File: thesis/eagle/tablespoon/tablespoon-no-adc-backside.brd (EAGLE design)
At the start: 106.3 x 71.1 mm, 35 parts, among them IC1 7805DT, IC2 7805DT, IC3 TL072D, U2 ADCS7477

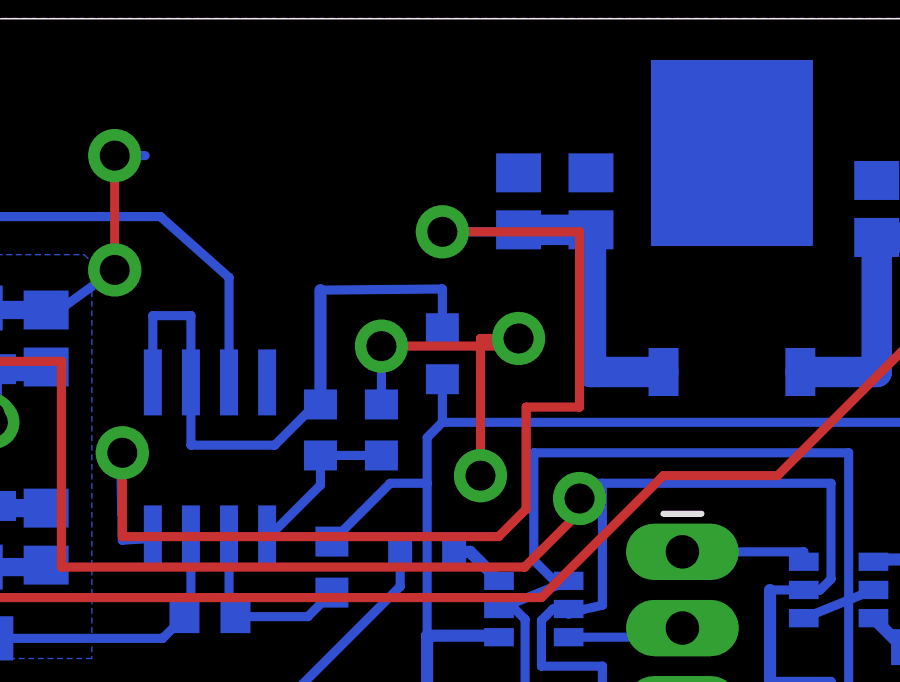
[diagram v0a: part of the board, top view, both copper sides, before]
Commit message: fixed lack of resistor divider on current amp
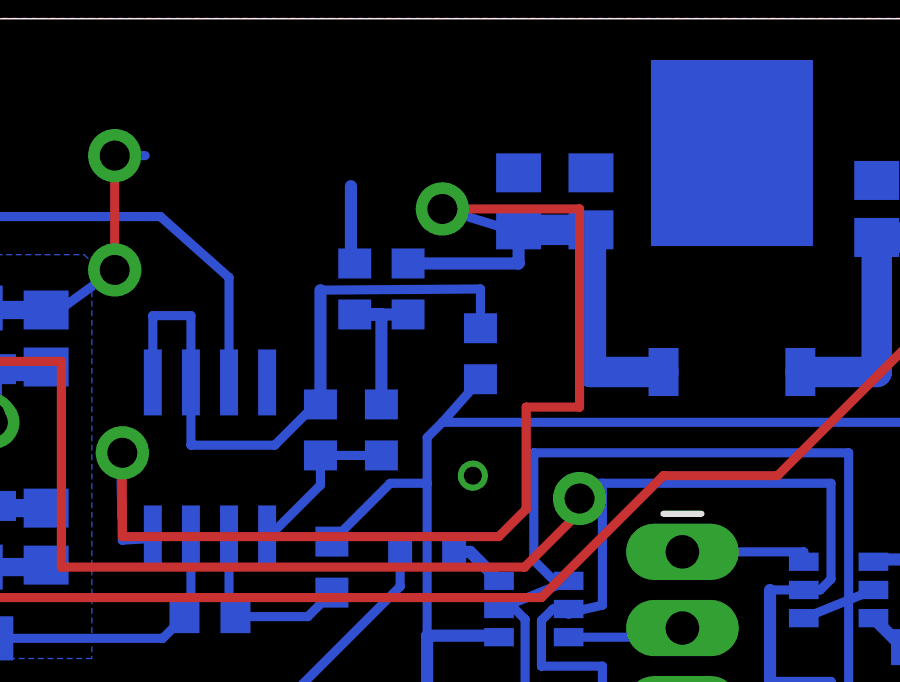
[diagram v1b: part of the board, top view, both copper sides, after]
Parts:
- added R14, R15: (no value), rcl:R0603
- moved R1 1.27 mm to (85.3, 59.9)
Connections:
- new net N$35: R14.1, R15.2, R3.1
- net 5V: now also R14.2
- net GND: now also R15.1; no longer R3.1
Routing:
- net GND: track 100.3 -> 90.6 mm, vias 5 -> 3
- net 5V: track 48.3 -> 54.0 mm
- net N$35: track 0.00 -> 5.67 mm
- net N$8: track 25.7 -> 27.0 mm

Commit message: going for the full-system on one board!
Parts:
- added M1, M2, M3, M4, M5, M6, M7, M8: (no value), butter:SOT23-3
- added R16, R17: (no value), SparkFun-Passives:0805
- added U$11: 4051", butter:TSSOP-16
- added U$2: RAILSEP, butter:RAIL
- added U1: ADCS7477, butter:SOT-23-6
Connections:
- removed net N$10: JP1.3, U$8.P$6
- removed net N$11: JP1.1, U$10.P$6
- removed net N$12: JP1.2, U$9.P$6
- removed net N$27: JP1.6, U$5.P$6
- removed net N$28: JP1.7, U$4.P$6
- new net N$1: JP1.2, M7.3, U$11.P$13, U$9.P$6
- new net N$36: R16.2, R17.2, U$10.P$5, U$3.P$5, U$4.P$5, U$5.P$5, U$6.P$5, U$7.P$5, U$8.P$5, U$9.P$5
- new net N$37: U$11.P$3, U1.P$3
- new net N$38: JP1.7, M2.3, U$11.P$4, U$4.P$6
- new net N$39: JP1.6, M3.3, U$11.P$2, U$5.P$6
- new net N$40: JP1.5, M4.3, U$11.P$1, U$6.P$6
- new net N$41: JP1.4, M5.3, U$11.P$15, U$7.P$6
- net !CS: now also U$1.P$12, U1.P$6; no longer U$1.P$62
- net 4.6V: now also R16.1; no longer U$10.P$5, U$3.P$5, U$4.P$5, U$5.P$5, U$6.P$5, U$7.P$5, U$8.P$5, U$9.P$5
- net 5V: now also R17.1, U$11.P$16
- net CK: now also U1.P$4
- net D0: now also U1.P$5
- net G0: now also M1.1
- net G1: now also M2.1
- net G2: now also M3.1
- net G3: now also M4.1
- net G4: now also M5.1
- net G5: now also M6.1
- net G6: now also M7.1
- net G7: now also M8.1
- net GND: now also M1.2, M2.2, M3.2, M4.2, M5.2, M6.2, M7.2, M8.2, U$11.P$7, U$11.P$8, U1.P$2
- net N$2: now also U1.P$1
- net N$29: now also M1.3, U$11.P$5
- net N$6: now also JP1.3, M6.3, U$11.P$14, U$8.P$6; no longer JP1.4, U$7.P$6
- net N$9: now also JP1.1, M8.3, U$10.P$6, U$11.P$12; no longer JP1.5, U$6.P$6
- net S0: now also U$11.P$11
- net S1: now also U$11.P$10
- net S2: now also U$11.P$9
- net SE: now also U$11.P$6
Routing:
- net G0: track 0.00 -> 82.5 mm
- net G1: track 0.00 -> 77.7 mm
- net N$36: track 0.00 -> 75.6 mm, vias 0 -> 1
- net G2: track 0.00 -> 73.7 mm
- net 4.6V: track 116.3 -> 46.4 mm, vias 1 -> 0
- net G3: track 0.00 -> 68.8 mm
- net G4: track 0.00 -> 65.1 mm
- net G5: track 0.00 -> 59.8 mm
- net G6: track 0.00 -> 56.3 mm
- net !CS: track 12.9 -> 63.7 mm, vias 0 -> 1
- net CK: track 50.3 -> 0.00 mm, vias 2 -> 0
- net G7: track 0.00 -> 49.1 mm
- net GND: track 90.6 -> 130.0 mm
- net N$38: track 0.00 -> 23.3 mm
- net N$9: track 4.10 -> 25.6 mm
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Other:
- board size 106.3 x 71.1 mm -> 107.4 x 71.9 mm

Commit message: finished new board
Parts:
- added JP2: POWER_JACKPTH, SparkFun-Connectors:POWER_JACK_PTH
- moved C2 3.59 mm to (67.3, 57.9)
- moved U2 3.59 mm to (68.1, 45.7)
- moved IC2 3.59 mm to (63.8, 53.6)
- moved C1 3.59 mm to (67.3, 49.3)
- moved C3 3.59 mm to (70.4, 56.9)
- moved C4 3.59 mm to (70.4, 50.3)
- moved U1 1.70 mm to (74.7, 45.7), flipped to the bottom, turned to 270 degrees
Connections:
- net GND: now also JP2.GND, JP2.GNDBREAK, U$1.P$1, U$1.P$2, U$1.P$49, U$1.P$50
- net N$5: now also JP2.PWR
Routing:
- net CK: track 0.00 -> 71.4 mm, vias 0 -> 2
- net SE: track 0.00 -> 34.9 mm, vias 0 -> 2
- net S0: track 0.00 -> 33.2 mm
- net S1: track 0.00 -> 28.7 mm
- net S2: track 0.00 -> 28.5 mm
- net D0: track 0.00 -> 24.5 mm
- net GND: track 130.0 -> 147.5 mm, vias 3 -> 5
- net !CS: track 63.7 -> 76.4 mm, vias 1 -> 2
- net N$37: track 0.00 -> 9.68 mm, vias 0 -> 1
- net N$2: track 8.80 -> 15.4 mm
- net 4.6V: track 46.4 -> 42.4 mm
- net CUR: track 8.94 -> 11.3 mm, vias 0 -> 2
- net 5V: track 51.8 -> 53.5 mm
- net D1: track 15.4 -> 13.8 mm
- net N$5: track 68.1 -> 66.6 mm, vias 3 -> 1
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- added copper zone on layer 1, net 5V
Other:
- board size 107.4 x 71.9 mm -> 107.4 x 71.1 mm
